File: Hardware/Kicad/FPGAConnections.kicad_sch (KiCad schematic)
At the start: 63 parts, among them U2 XC6SLX9-TQG144

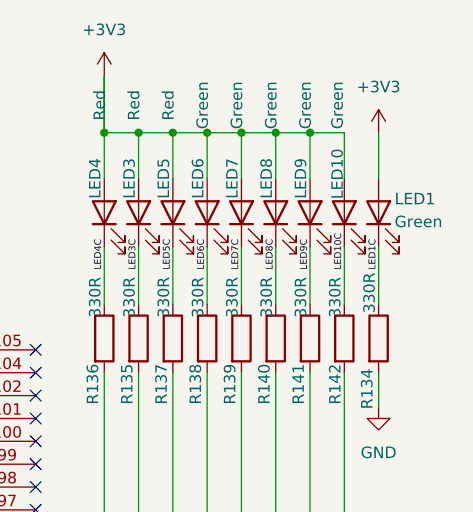
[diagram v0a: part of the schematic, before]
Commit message: Swapped LED1 and LED2
1) Swapped LED1 and LED2 identifiers to be consistent with original schematic and correct color in BOM
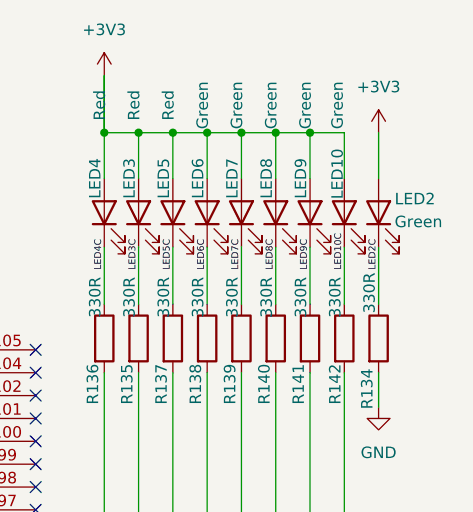
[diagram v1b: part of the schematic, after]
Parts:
- renumbered LED1 to LED2
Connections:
- net LED1C renamed LED2C
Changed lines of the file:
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@@
 		)
 	)
-	(label "LED1C"
+	(label "LED2C"
 		(at 393.7 40.64 90)
 		(fields_autoplaced yes)
@@
 		(on_board yes)
 		(dnp no)
-		(property "Reference" "LED1"
+		(property "Reference" "LED2"
 			(at 395.478 32.766 90)
 			(effects
@@
 			(project "VNA"
 				(path "/7469840a-34dd-443e-8d3c-7bb0beac8ed2/798b71c1-ee2e-4e21-b7d2-78d3e660f322"
-					(reference "LED1")
+					(reference "LED2")
 					(unit 1)
 				)
